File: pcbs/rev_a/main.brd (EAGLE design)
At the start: 71.3 x 49 mm, 16 parts

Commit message: First candidate board
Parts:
- added R4: 2K, resistor:0309V
- added R6: 1K, resistor:0309V
- R1, R2: value (none) -> 10K
- moved JP4 0.25 mm to (2.54, 32.3)
- moved JP2 0.25 mm to (-1.52, 15.2)
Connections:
- removed net N$34: C1.2, JP1.5, JP2.3, JP3.5, JP5.4, R1.1, U$1.JP2.7, U$7.PB_P0
- new net N$16: C1.2, JP1.5, JP2.3, JP3.5, JP5.1, R1.1, R4.2, U$1.JP2.7, U$7.PB_P0
- new net N$9: JP5.2, R4.1, R6.2
- net N$1: no longer JP5.1
- net N$11: now also R6.1; no longer JP5.2
- net N$2: now also JP5.4
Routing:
- net N$16: track 0.00 -> 171.0 mm, vias 0 -> 6
- net N$10: track 0.00 -> 138.2 mm, vias 0 -> 2
- net N$2: track 55.5 -> 101.5 mm
- net N$34: track 34.3 -> 0.00 mm
- net N$6: track 0.00 -> 28.5 mm
- net N$3: track 0.00 -> 22.0 mm
- net N$5: track 0.00 -> 15.7 mm
- net N$7: track 0.00 -> 15.5 mm
- net N$12: track 0.00 -> 11.6 mm
- net N$14: track 0.00 -> 8.63 mm
- net N$9: track 0.00 -> 7.91 mm
- net N$11: track 0.00 -> 5.39 mm
- net N$8: track 0.00 -> 2.90 mm
- net N$1: track 127.8 -> 128.5 mm

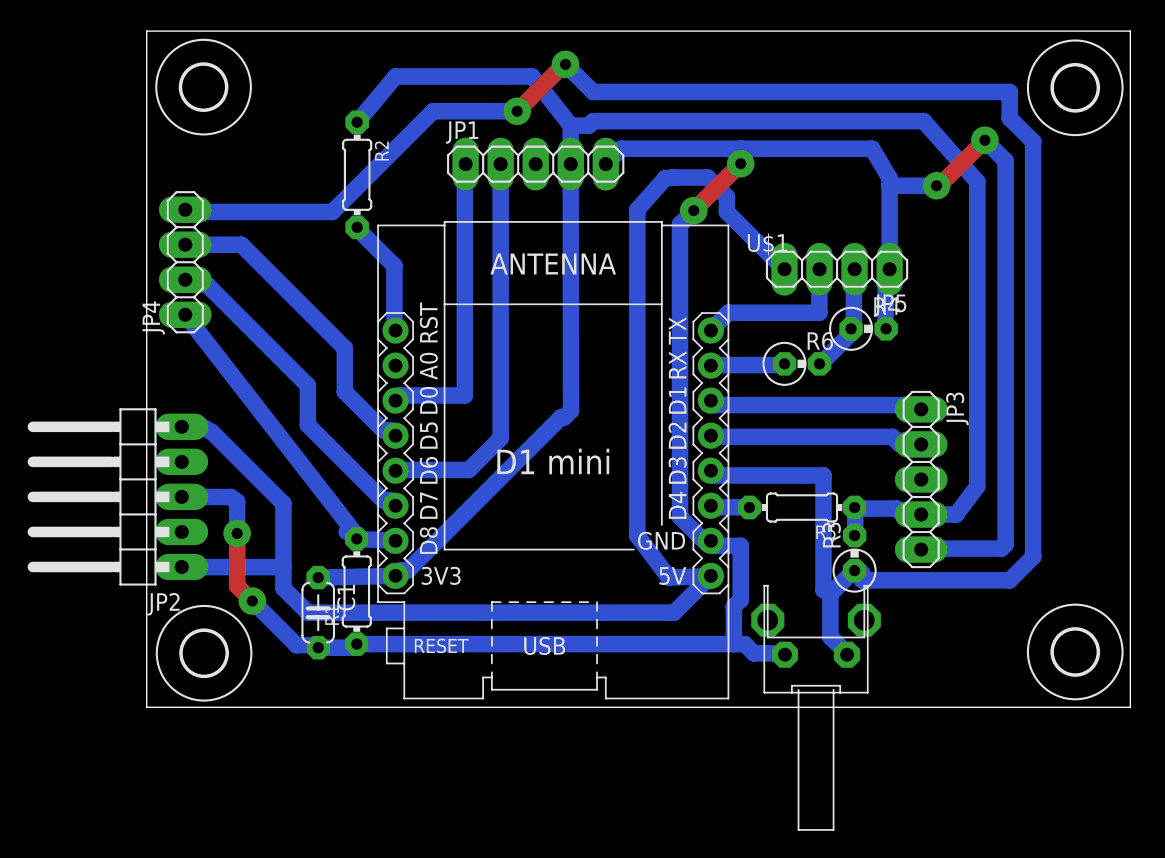
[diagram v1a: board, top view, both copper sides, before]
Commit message: Work on PCB and firmware updates for the SR04 range finder - Move PCB pinouts.  I wasn't able to use the TX or RX pins as inputs - Add a WS2812 plug.  It might be usable with the last port, and it does no harm - Work on the firmware for the SR04.  Firmware can not find successfully return ranges.  Reliability still needs work
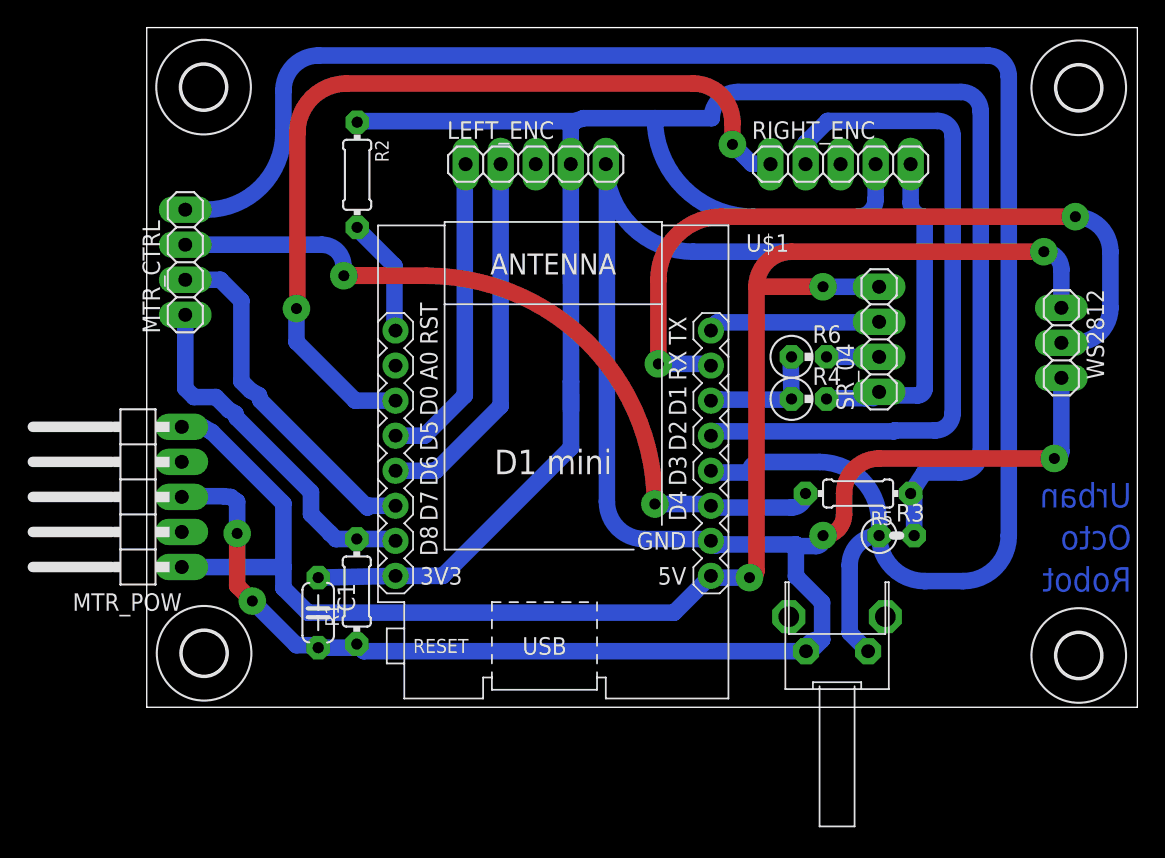
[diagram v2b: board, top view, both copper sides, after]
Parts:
- removed JP3: (no value), pinhead:1X05
- removed JP5: (no value), pinhead:1X04
- added RIGHT_ENC: (no value), pinhead:1X05
- added SR_04: (no value), pinhead:1X04
- added WS2812: (no value), pinhead:1X03
- R3: device resistor:0309V -> resistor:0207/2V
- R5: value (none) -> 10K
- moved R4 6.67 mm to (47.8, 22.4)
- moved R5 4.19 mm to (51.3, 15.5)
- moved R3 3.30 mm to (54.1, 12.4), turned to 0 degrees
- moved U$7 1.55 mm to (49.8, 4.06)
- moved R6 0.72 mm to (47.8, 25.4)
- moved U$5 0.36 mm to (67.3, 3.75)
- moved U$3 0.25 mm to (67.3, 44.9)
- renumbered JP1 to LEFT_ENC, JP2 to MTR_POW, JP4 to MTR_CTRL
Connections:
- net N$1: now also U$1.JP2.2, WS2812.2; no longer C1.1, JP3.4, LEFT_ENC.4, R2.1, R3.2, R5.1, U$1.JP1.8
- net N$11: now also R4.1, U$1.JP2.3; no longer U$1.JP2.2
- net N$12: now also SR_04.3; no longer JP5.3
- net N$13: now also R5.2, U$1.JP2.6; no longer U$1.JP1.4
- net N$16: now also RIGHT_ENC.5, SR_04.1, WS2812.3; no longer JP3.5, JP5.1
- net N$2: now also SR_04.4, WS2812.1; no longer JP5.4
- net N$3: now also U$1.JP1.4; no longer U$1.JP1.3
- net N$5: now also RIGHT_ENC.2, U$1.JP2.4; no longer JP3.1, U$1.JP2.3
- net N$7: now also RIGHT_ENC.1, U$1.JP1.3; no longer JP3.2, U$1.JP2.4
- net N$8: now also C1.1, LEFT_ENC.4, R2.1, R3.2, R5.1, RIGHT_ENC.4, U$1.JP1.8; no longer R5.2, U$1.JP2.6
- net N$9: now also SR_04.2; no longer JP5.2, R4.1
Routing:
- net N$8: track 2.90 -> 151.1 mm
- net N$1: track 128.5 -> 54.9 mm, vias 0 -> 2
- net N$7: track 15.5 -> 63.2 mm, vias 0 -> 2
- net N$5: track 15.7 -> 51.6 mm
- net N$13: track 22.8 -> 56.6 mm, vias 0 -> 2
- net N$2: track 101.5 -> 115.7 mm, vias 0 -> 3
- net N$16: track 171.0 -> 183.9 mm, vias 6 -> 4
- net N$11: track 5.39 -> 9.10 mm
- net N$9: track 7.91 -> 4.60 mm
- net N$4: track 23.7 -> 25.6 mm
- net N$15: track 24.3 -> 26.2 mm
- net N$6: track 28.5 -> 27.1 mm
- net N$3: track 22.0 -> 23.0 mm
- net N$12: track 11.6 -> 12.6 mm
- net N$10: track 138.2 -> 137.5 mm, vias 2 -> 0
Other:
- board size 71.3 x 49 mm -> 71.8 x 49.3 mm
- board text added: "Octo"
- board text added: "Robot"
- board text added: "Urban"

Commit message: Move GPIOs so the firmware can (hopefully) use interrupts instead of polling in encoders.
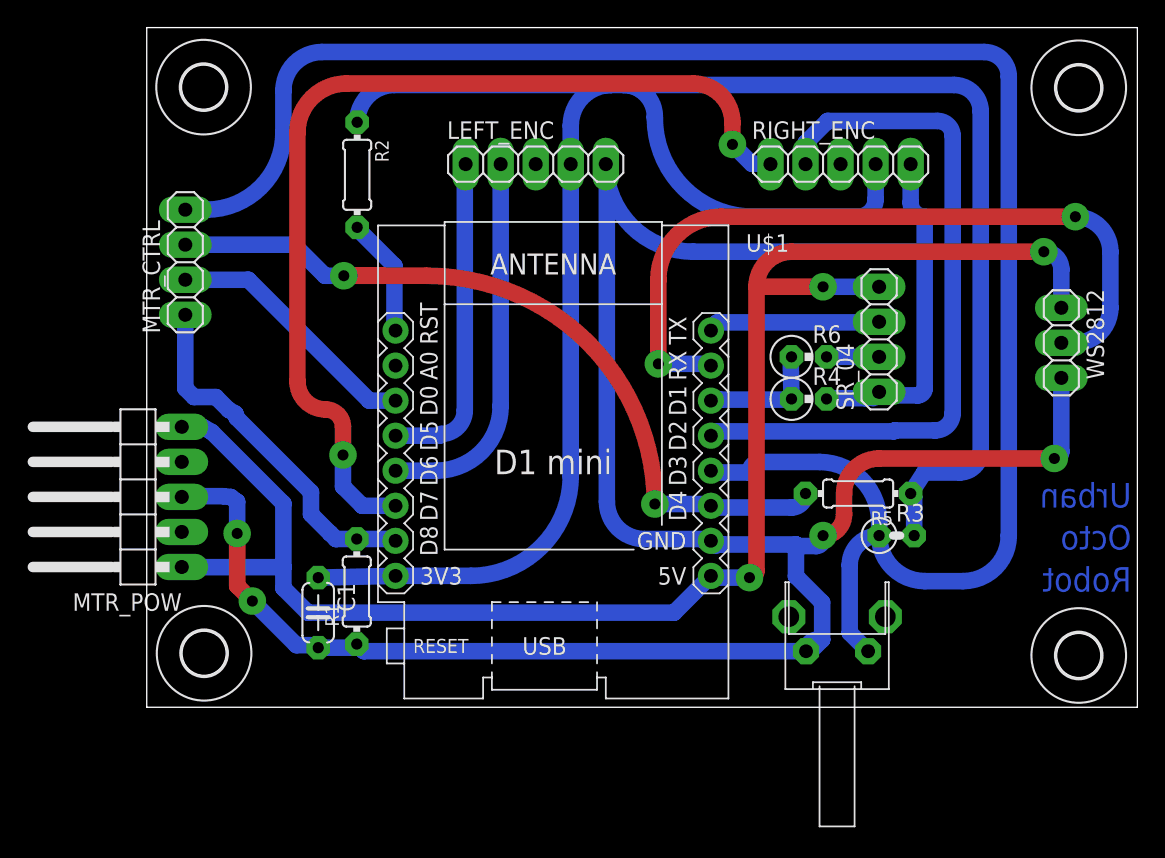
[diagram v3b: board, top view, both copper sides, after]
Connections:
- net N$4: now also U$1.JP1.3; no longer U$1.JP1.6
- net N$7: now also U$1.JP1.6; no longer U$1.JP1.3
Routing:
- net N$7: track 63.2 -> 70.5 mm
- net N$4: track 25.6 -> 18.9 mm
- net N$8: track 151.1 -> 157.7 mm
- net N$3: track 23.0 -> 23.6 mm
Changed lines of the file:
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@@
 <wire x1="48.514" y1="17.78" x2="52.832" y2="13.462" width="1.2" layer="16" curve="-90"/>
 <wire x1="52.832" y1="13.462" x2="52.832" y2="12.446" width="1.2" layer="16"/>
-<wire x1="9.652" y1="44.704" x2="12.192" y2="47.244" width="1.2" layer="16" curve="-90"/>
-<wire x1="12.192" y1="47.244" x2="60.706" y2="47.244" width="1.2" layer="16"/>
-<wire x1="60.706" y1="47.244" x2="62.23" y2="45.72" width="1.2" layer="16" curve="-90"/>
+<wire x1="9.652" y1="44.704" x2="12.446" y2="47.498" width="1.2" layer="16" curve="-90"/>
+<wire x1="12.446" y1="47.498" x2="60.452" y2="47.498" width="1.2" layer="16"/>
+<wire x1="60.452" y1="47.498" x2="62.23" y2="45.72" width="1.2" layer="16" curve="-90"/>
 <wire x1="62.23" y1="45.72" x2="62.23" y2="12.446" width="1.2" layer="16"/>
 <contactref element="U$7" pad="PB_P1"/>
@@
 <signal name="N$3">
 <contactref element="LEFT_ENC" pad="1"/>
-<wire x1="22.8" y1="22.6" x2="22.8" y2="39.3" width="1.2" layer="16"/>
+<wire x1="22.8" y1="21.53" x2="22.8" y2="39.3" width="1.2" layer="16"/>
 <wire x1="22.8" y1="39.3" x2="22.86" y2="39.37" width="1.2" layer="16"/>
 <contactref element="U$1" pad="JP1.4"/>
-<wire x1="17.78" y1="19.685" x2="19.885" y2="19.685" width="1.2" layer="16"/>
-<wire x1="19.885" y1="19.685" x2="22.8" y2="22.6" width="1.2" layer="16"/>
-</signal>
-<signal name="N$4">
-<contactref element="U$1" pad="JP1.6"/>
-<contactref element="MTR_CTRL" pad="2"/>
-<wire x1="2.54" y1="30.988" x2="5.08" y2="30.988" width="1.2" layer="16"/>
-<wire x1="6.604" y1="29.464" x2="5.08" y2="30.988" width="1.2" layer="16"/>
-<wire x1="17.78" y1="14.605" x2="15.875" y2="14.605" width="1.2" layer="16"/>
-<wire x1="15.875" y1="14.605" x2="15.748" y2="14.478" width="1.2" layer="16"/>
-<wire x1="15.748" y1="14.478" x2="7.986059375" y2="22.239940625" width="1.2" layer="16"/>
-<wire x1="7.986059375" y1="22.239940625" x2="7.8817875" y2="22.61461875" width="1.2" layer="16"/>
-<wire x1="7.8817875" y1="22.61461875" x2="7.260753125" y2="22.965246875" width="1.2" layer="16"/>
-<wire x1="7.260753125" y1="22.965246875" x2="6.604" y2="23.622" width="1.2" layer="16"/>
-<wire x1="6.604" y1="23.622" x2="6.604" y2="29.464" width="1.2" layer="16"/>
+<wire x1="20.955" y1="19.685" x2="21.082" y2="19.812" width="1.2" layer="16" curve="90"/>
+<wire x1="21.082" y1="19.812" x2="22.8" y2="21.53" width="1.2" layer="16" curve="90"/>
+<wire x1="17.78" y1="19.685" x2="20.955" y2="19.685" width="1.2" layer="16"/>
 </signal>
 <signal name="N$11">
@@
 </signal>
 <signal name="N$7">
-<contactref element="U$1" pad="JP1.3"/>
 <contactref element="RIGHT_ENC" pad="1"/>
 <wire x1="43.6" y1="39.4" x2="42.2" y2="40.8" width="1.2" layer="16"/>
 <wire x1="44.9" y1="39.4" x2="43.6" y2="39.4" width="1.2" layer="16"/>
 <wire x1="44.9" y1="39.4" x2="44.958" y2="39.37" width="1.2" layer="16"/>
-<via x="10.6" y="28.9" extent="1-16" drill="0.8"/>
 <via x="42.2" y="40.8" extent="1-16" drill="0.8"/>
-<wire x1="10.6" y1="28.9" x2="10.668" y2="28.968" width="1.2" layer="1" curve="90"/>
-<wire x1="10.668" y1="28.968" x2="10.668" y2="41.656" width="1.2" layer="1"/>
 <wire x1="10.668" y1="41.656" x2="14.224" y2="45.212" width="1.2" layer="1" curve="-90"/>
 <wire x1="39.37" y1="45.212" x2="42.2" y2="42.382" width="1.2" layer="1" curve="-90"/>
 <wire x1="42.2" y1="42.382" x2="42.2" y2="40.8" width="1.2" layer="1"/>
 <wire x1="14.224" y1="45.212" x2="39.37" y2="45.212" width="1.2" layer="1"/>
-<wire x1="17.78" y1="22.225" x2="14.859" y2="22.225" width="1.2" layer="16"/>
-<wire x1="10.6" y1="26.484" x2="10.6" y2="28.9" width="1.2" layer="16"/>
-<wire x1="14.859" y1="22.225" x2="10.6" y2="26.484" width="1.2" layer="16"/>
+<contactref element="U$1" pad="JP1.6"/>
+<wire x1="17.78" y1="14.605" x2="15.367" y2="14.605" width="1.2" layer="16"/>
+<wire x1="13.97" y1="16.002" x2="13.97" y2="18.288" width="1.2" layer="16"/>
+<wire x1="15.367" y1="14.605" x2="13.97" y2="16.002" width="1.2" layer="16"/>
+<via x="13.97" y="18.288" extent="1-16" drill="0.8"/>
+<wire x1="13.97" y1="18.288" x2="13.97" y2="20.32" width="1.2" layer="1"/>
+<wire x1="13.97" y1="20.32" x2="12.7" y2="21.59" width="1.2" layer="1" curve="90"/>
+<wire x1="12.7" y1="21.59" x2="10.668" y2="23.622" width="1.2" layer="1" curve="-90"/>
+<wire x1="10.668" y1="23.622" x2="10.668" y2="41.656" width="1.2" layer="1"/>
 </signal>
 <signal name="N$6">
@@
 <wire x1="25.4" y1="39.37" x2="25.4" y2="21.844" width="1.2" layer="16"/>
 <wire x1="20.701" y1="17.145" x2="17.78" y2="17.145" width="1.2" layer="16"/>
-<wire x1="25.4" y1="21.844" x2="20.701" y2="17.145" width="1.2" layer="16"/>
+<wire x1="25.4" y1="21.844" x2="20.701" y2="17.145" width="1.2" layer="16" curve="-90"/>
 </signal>
 <signal name="N$5">
@@
 <wire x1="40.513" y1="14.732" x2="36.576" y2="14.732" width="1.2" layer="16"/>
 <via x="36.576" y="14.732" extent="1-16" drill="0.8"/>
-<wire x1="2.6" y1="33.5" x2="2.54" y2="33.528" width="1.2" layer="16"/>
 <wire x1="36.576" y1="14.732" x2="20.03" y2="31.278" width="1.2" layer="1" curve="90"/>
 <wire x1="20.03" y1="31.278" x2="14.03" y2="31.278" width="1.2" layer="1"/>
-<wire x1="12.446" y1="33.528" x2="14.008" y2="31.966" width="1.2" layer="16" curve="-90"/>
-<wire x1="14.008" y1="31.966" x2="14.008" y2="31.3" width="1.2" layer="16"/>
-<wire x1="2.54" y1="33.528" x2="12.446" y2="33.528" width="1.2" layer="16"/>
+<wire x1="12.664" y1="31.278" x2="14.03" y2="31.278" width="1.2" layer="16"/>
+<wire x1="2.54" y1="33.528" x2="10.414" y2="33.528" width="1.2" layer="16"/>
+<wire x1="10.414" y1="33.528" x2="12.664" y2="31.278" width="1.2" layer="16"/>
 </signal>
 <signal name="N$16">
@@
 <contactref element="R2" pad="1"/>
 <contactref element="RIGHT_ENC" pad="4"/>
-<wire x1="30.5" y1="21.5" x2="30.497625" y2="23.622303125" width="1.2" layer="16"/>
-<wire x1="30.497625" y1="23.622303125" x2="30.48" y2="39.37" width="1.2" layer="16"/>
 <wire x1="30.48" y1="39.37" x2="30.48" y2="42.164" width="1.2" layer="16"/>
-<wire x1="30.48" y1="42.164" x2="30.802" y2="42.486" width="1.2" layer="16"/>
-<wire x1="30.802" y1="42.486" x2="15.08" y2="42.486" width="1.2" layer="16"/>
-<wire x1="15.08" y1="42.486" x2="15" y2="42.406" width="1.2" layer="16"/>
-<wire x1="31.4" y1="42.7" x2="36.576" y2="42.7" width="1.2" layer="16"/>
-<wire x1="36.576" y1="42.7" x2="40.7" y2="42.7" width="1.2" layer="16"/>
-<wire x1="31.4" y1="42.7" x2="30.802" y2="42.486" width="1.2" layer="16"/>
 <wire x1="56.099453125" y1="17.018" x2="55.118" y2="15.494" width="1.2" layer="16"/>
 <wire x1="56.099453125" y1="17.018" x2="58.674" y2="17.018" width="1.2" layer="16"/>
 <wire x1="58.674" y1="17.018" x2="60.198" y2="18.542" width="1.2" layer="16" curve="90"/>
-<wire x1="58.778" y1="44.6" x2="60.198" y2="43.18" width="1.2" layer="16" curve="-90"/>
+<wire x1="60.198" y1="43.18" x2="58.27" y2="45.108" width="1.2" layer="16" curve="90"/>
 <wire x1="60.198" y1="18.542" x2="60.198" y2="43.18" width="1.2" layer="16"/>
 <wire x1="55.118" y1="15.494" x2="55.372" y2="15.24" width="1.2" layer="16" curve="-90"/>
 <wire x1="55.372" y1="15.24" x2="55.372" y2="12.446" width="1.2" layer="16"/>
-<wire x1="42.6" y1="44.6" x2="58.778" y2="44.6" width="1.2" layer="16"/>
-<wire x1="40.7" y1="42.7" x2="42.6" y2="44.6" width="1.2" layer="16" curve="-90"/>
-<wire x1="36.576" y1="42.7" x2="43.716" y2="35.56" width="1.2" layer="16" curve="90"/>
+<wire x1="43.716" y1="35.56" x2="36.576" y2="42.7" width="1.2" layer="16" curve="-90"/>
 <wire x1="43.716" y1="35.56" x2="51.308" y2="35.56" width="1.2" layer="16"/>
 <wire x1="51.308" y1="35.56" x2="52.578" y2="36.83" width="1.2" layer="16" curve="90"/>
 <wire x1="52.578" y1="36.83" x2="52.578" y2="39.37" width="1.2" layer="16"/>
 <wire x1="17.8" y1="9.5" x2="17.78" y2="9.525" width="1.2" layer="16"/>
-<wire x1="17.78" y1="9.525" x2="21.209" y2="9.525" width="1.2" layer="16"/>
-<wire x1="30.497625" y1="18.813625" x2="30.497625" y2="23.622303125" width="1.2" layer="16"/>
-<wire x1="21.209" y1="9.525" x2="30.497625" y2="18.813625" width="1.2" layer="16"/>
+<wire x1="33.424" y1="45.108" x2="30.48" y2="42.164" width="1.2" layer="16" curve="90"/>
+<wire x1="58.27" y1="45.108" x2="34.29" y2="45.108" width="1.2" layer="16"/>
+<wire x1="34.29" y1="45.108" x2="33.424" y2="45.108" width="1.2" layer="16"/>
+<wire x1="36.576" y1="42.7" x2="36.576" y2="42.822" width="1.2" layer="16"/>
+<wire x1="36.576" y1="42.822" x2="34.29" y2="45.108" width="1.2" layer="16" curve="90"/>
+<wire x1="33.424" y1="45.108" x2="17.702" y2="45.108" width="1.2" layer="16"/>
+<wire x1="17.702" y1="45.108" x2="15" y2="42.406" width="1.2" layer="16" curve="90"/>
+<wire x1="17.78" y1="9.525" x2="23.241" y2="9.525" width="1.2" layer="16"/>
+<wire x1="23.241" y1="9.525" x2="30.48" y2="16.764" width="1.2" layer="16" curve="90"/>
+<wire x1="30.48" y1="16.764" x2="30.48" y2="39.37" width="1.2" layer="16"/>
 </signal>
 <signal name="N$1">
@@
 <wire x1="67.056" y1="35.56" x2="41.402" y2="35.56" width="1.2" layer="1"/>
 </signal>
+<signal name="N$4">
+<contactref element="U$1" pad="JP1.3"/>
+<contactref element="MTR_CTRL" pad="2"/>
+<wire x1="2.54" y1="30.988" x2="7.112" y2="30.988" width="1.2" layer="16"/>
+<wire x1="7.112" y1="30.988" x2="15.875" y2="22.225" width="1.2" layer="16"/>
+<wire x1="15.875" y1="22.225" x2="17.78" y2="22.225" width="1.2" layer="16"/>
+</signal>
 </signals>
